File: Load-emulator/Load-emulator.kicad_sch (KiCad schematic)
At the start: 16 parts, among them J1 87832-1420, J2 SSW-126-04-G-D, J3 SSW-126-04-G-D, Q1 TIP41C, U1 LM324A

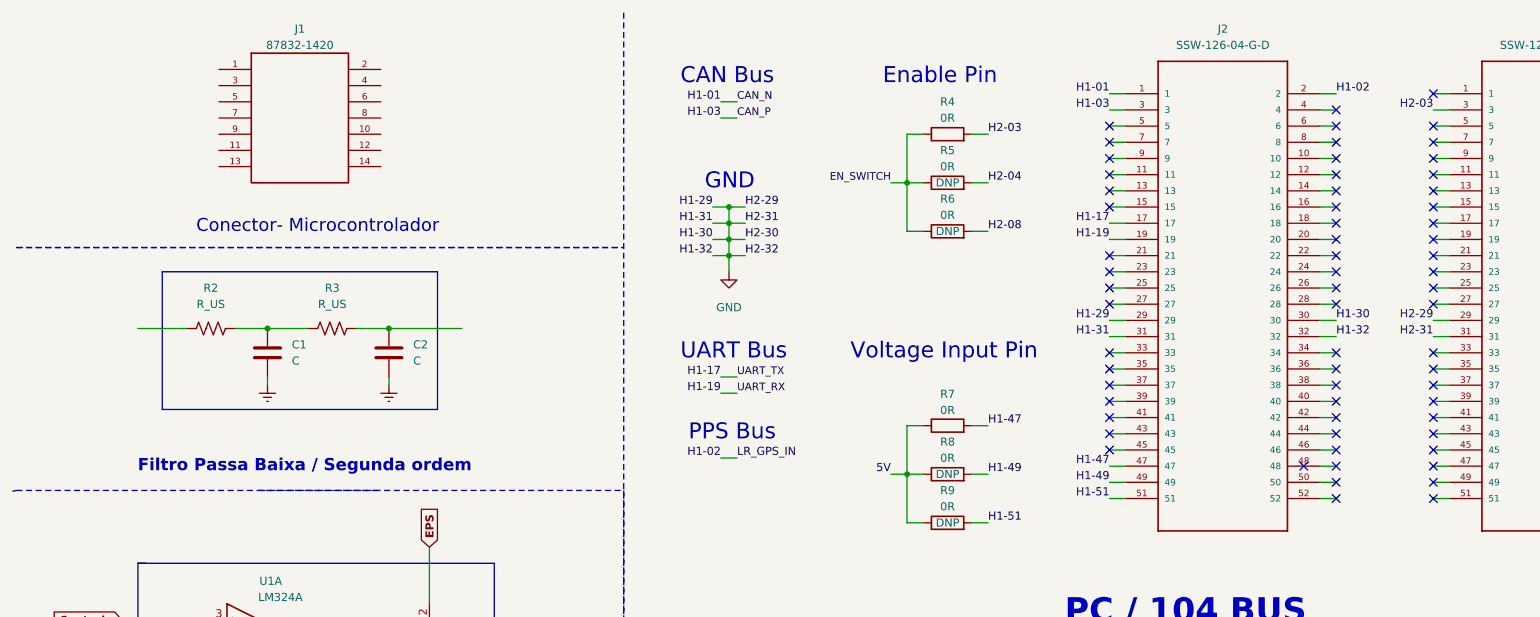
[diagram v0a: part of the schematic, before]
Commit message: Named the connections of PC-104 according to the loads we're trying to emulate
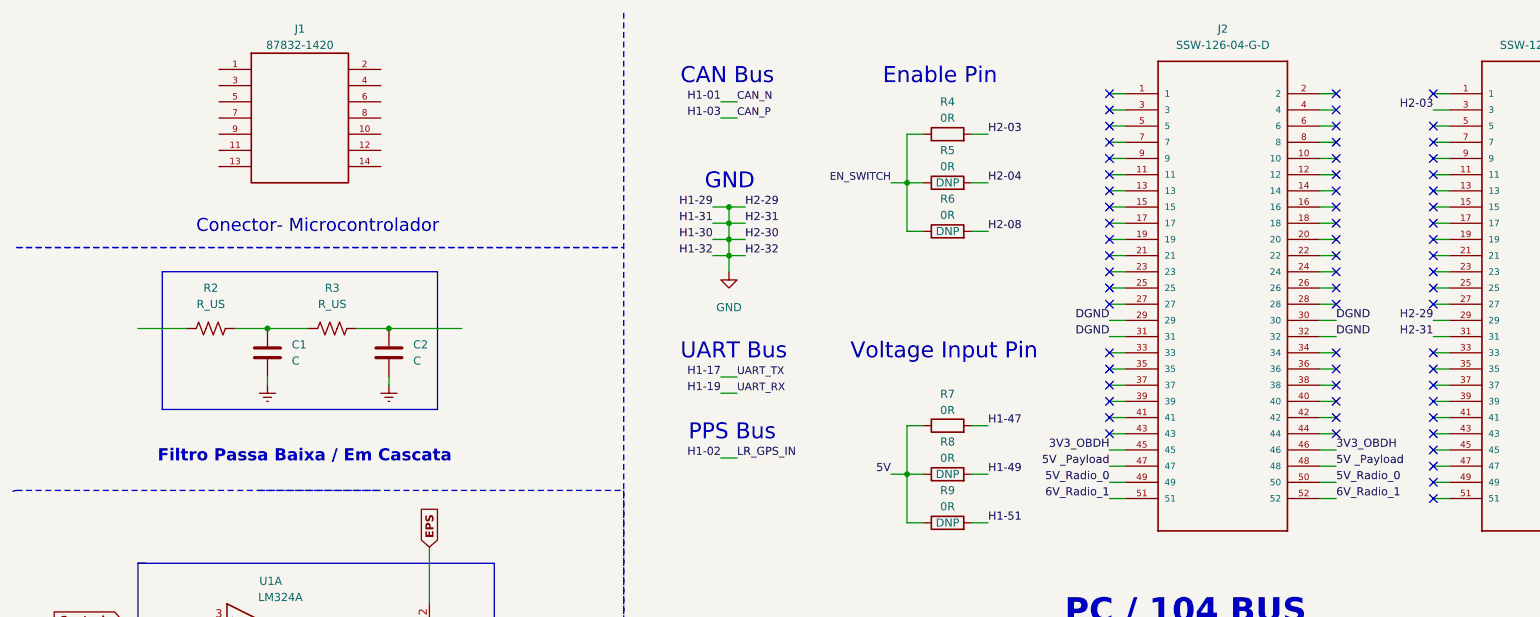
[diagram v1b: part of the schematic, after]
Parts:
- J2: footprint lib:TSW-126-07-X-D -> footprints:SSW-126-01-G-D
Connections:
- net CAN_N: no longer J2.1
- net CAN_P: no longer J2.3
- net GND: no longer J2.29, J2.30, J2.31, J2.32
- net H1-02: no longer J2.2
- net H1-17: no longer J2.17
- net H1-19: no longer J2.19
- net H1-47: no longer J2.47
- net H1-49: no longer J2.49
- net H1-51: no longer J2.51
- net 3V3_OBDH: now reaches J2.45
- net 3V3_OBDH: now also J2.46
- net 5V _Payload: now reaches J2.48
- net 5V _Payload: now also J2.47
- net 5V_Radio_0: now reaches J2.50
- net 5V_Radio_0: now also J2.49
- net 6V_Radio_1: now reaches J2.52
- net 6V_Radio_1: now also J2.51
- new net DGND: J2.29, J2.30, J2.31, J2.32
- no-connect marks 86 -> 85
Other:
- note added: "Filtro Passa Baixa / Em Cascata"
- note removed: "Filtro Passa Baixa / Segunda ordem"
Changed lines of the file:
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@@
 	)
 	(no_connect
-		(at 219.71 83.82)
+		(at 184.15 48.26)
 	)
 	(no_connect
@@
 	)
 	(no_connect
+		(at 184.15 27.94)
+	)
+	(no_connect
 		(at 219.71 73.66)
 	)
@@
 	)
 	(no_connect
-		(at 214.63 83.82)
-	)
-	(no_connect
 		(at 219.71 66.04)
 	)
 	(no_connect
+		(at 184.15 25.4)
+	)
+	(no_connect
 		(at 234.95 83.82)
 	)
@@
 	)
 	(no_connect
+		(at 184.15 45.72)
+	)
+	(no_connect
 		(at 219.71 35.56)
 	)
@@
 	)
 	(no_connect
-		(at 184.15 81.28)
-	)
-	(no_connect
 		(at 219.71 55.88)
 	)
@@
 	)
 	(no_connect
-		(at 219.71 88.9)
-	)
-	(no_connect
 		(at 184.15 68.58)
 	)
@@
 	)
 	(no_connect
+		(at 219.71 25.4)
+	)
+	(no_connect
 		(at 270.51 88.9)
 	)
@@
 	)
 	(no_connect
-		(at 219.71 81.28)
-	)
-	(no_connect
 		(at 234.95 33.02)
 	)
@@
 	(no_connect
 		(at 234.95 35.56)
-	)
-	(no_connect
-		(at 219.71 86.36)
 	)
 	(no_connect
@@
 		)
 	)
-	(text "Filtro Passa Baixa / Segunda ordem\n"
+	(text "Filtro Passa Baixa / Em Cascata\n\n"
 		(exclude_from_sim no)
 		(at 57.912 83.82 0)
@@
 		)
 	)
-	(label "H1-47"
+	(label "5V _Payload"
 		(at 184.15 83.82 180)
 		(fields_autoplaced yes)
@@
 		)
 	)
-	(label "H1-32"
+	(label "DGND"
 		(at 219.71 63.5 0)
 		(fields_autoplaced yes)
@@
 		)
 	)
-	(label "H1-02"
-		(at 219.71 25.4 0)
-		(fields_autoplaced yes)
-		(effects
-			(font
-				(size 1.27 1.27)
-			)
-			(justify left bottom)
-		)
-	)
 	(label "H2-30"
 		(at 270.51 60.96 0)
@@
 		)
 	)
-	(label "H1-49"
+	(label "5V_Radio_0"
 		(at 184.15 86.36 180)
 		(fields_autoplaced yes)
@@
 		)
 	)
-	(label "H1-51"
+	(label "6V_Radio_1"
 		(at 184.15 88.9 180)
 		(fields_autoplaced yes)
@@
 		)
 	)
+	(label "3V3_OBDH"
+		(at 184.15 81.28 180)
+		(fields_autoplaced yes)
+		(effects
+			(font
+				(size 1.27 1.27)
+			)
+			(justify right bottom)
+		)
+	)
 	(label "H1-19"
 		(at 123.19 72.39 180)
@@
 	)
 	(label "H1-17"
-		(at 184.15 45.72 180)
-		(fields_autoplaced yes)
-		(effects
-			(font
-				(size 1.27 1.27)
-			)
-			(justify right bottom)
-		)
-	)
-	(label "H1-17"
 		(at 123.19 69.85 180)
 		(fields_autoplaced yes)
@@
 		)
 	)
+	(label "3V3_OBDH"
+		(at 219.71 81.28 0)
+		(fields_autoplaced yes)
+		(effects
+			(font
+				(size 1.27 1.27)
+			)
+			(justify left bottom)
+		)
+	)
 	(label "H2-04"
 		(at 165.1 39.37 0)
@@
 		)
 	)
-	(label "H1-01"
-		(at 184.15 25.4 180)
-		(fields_autoplaced yes)
-		(effects
-			(font
-				(size 1.27 1.27)
-			)
-			(justify right bottom)
-		)
-	)
-	(label "H1-30"
+	(label "DGND"
 		(at 219.71 60.96 0)
 		(fields_autoplaced yes)
@@
 		)
 	)
-	(label "H1-31"
+	(label "DGND"
 		(at 184.15 63.5 180)
-		(fields_autoplaced yes)
-		(effects
-			(font
-				(size 1.27 1.27)
-			)
-			(justify right bottom)
-		)
-	)
-	(label "H1-03"
-		(at 184.15 27.94 180)
 		(fields_autoplaced yes)
 		(effects
@@
 		)
 	)
-	(label "H1-29"
+	(label "5V_Radio_0"
+		(at 219.71 86.36 0)
+		(fields_autoplaced yes)
+		(effects
+			(font
+				(size 1.27 1.27)
+			)
+			(justify left bottom)
+		)
+	)
+	(label "DGND"
 		(at 184.15 60.96 180)
 		(fields_autoplaced yes)
@@
 		)
 	)
-	(label "H1-19"
-		(at 184.15 48.26 180)
-		(fields_autoplaced yes)
-		(effects
-			(font
-				(size 1.27 1.27)
-			)
-			(justify right bottom)
-		)
-	)
 	(label "CAN_P"
 		(at 125.73 29.21 0)
@@
 		)
 	)
+	(label "5V _Payload"
+		(at 219.71 83.82 0)
+		(fields_autoplaced yes)
+		(effects
+			(font
+				(size 1.27 1.27)
+			)
+			(justify left bottom)
+		)
+	)
 	(label "H2-03"
 		(at 234.95 27.94 180)
@@
 			)
 			(justify right bottom)
+		)
+	)
+	(label "6V_Radio_1"
+		(at 219.71 88.9 0)
+		(fields_autoplaced yes)
+		(effects
+			(font
+				(size 1.27 1.27)
+			)
+			(justify left bottom)
 		)
 	)
@@
 			)
 		)
-		(property "Footprint" "lib:TSW-126-07-X-D"
+		(property "Footprint" "footprints:SSW-126-01-G-D"
 			(at 191.77 25.4 0)
 			(effects

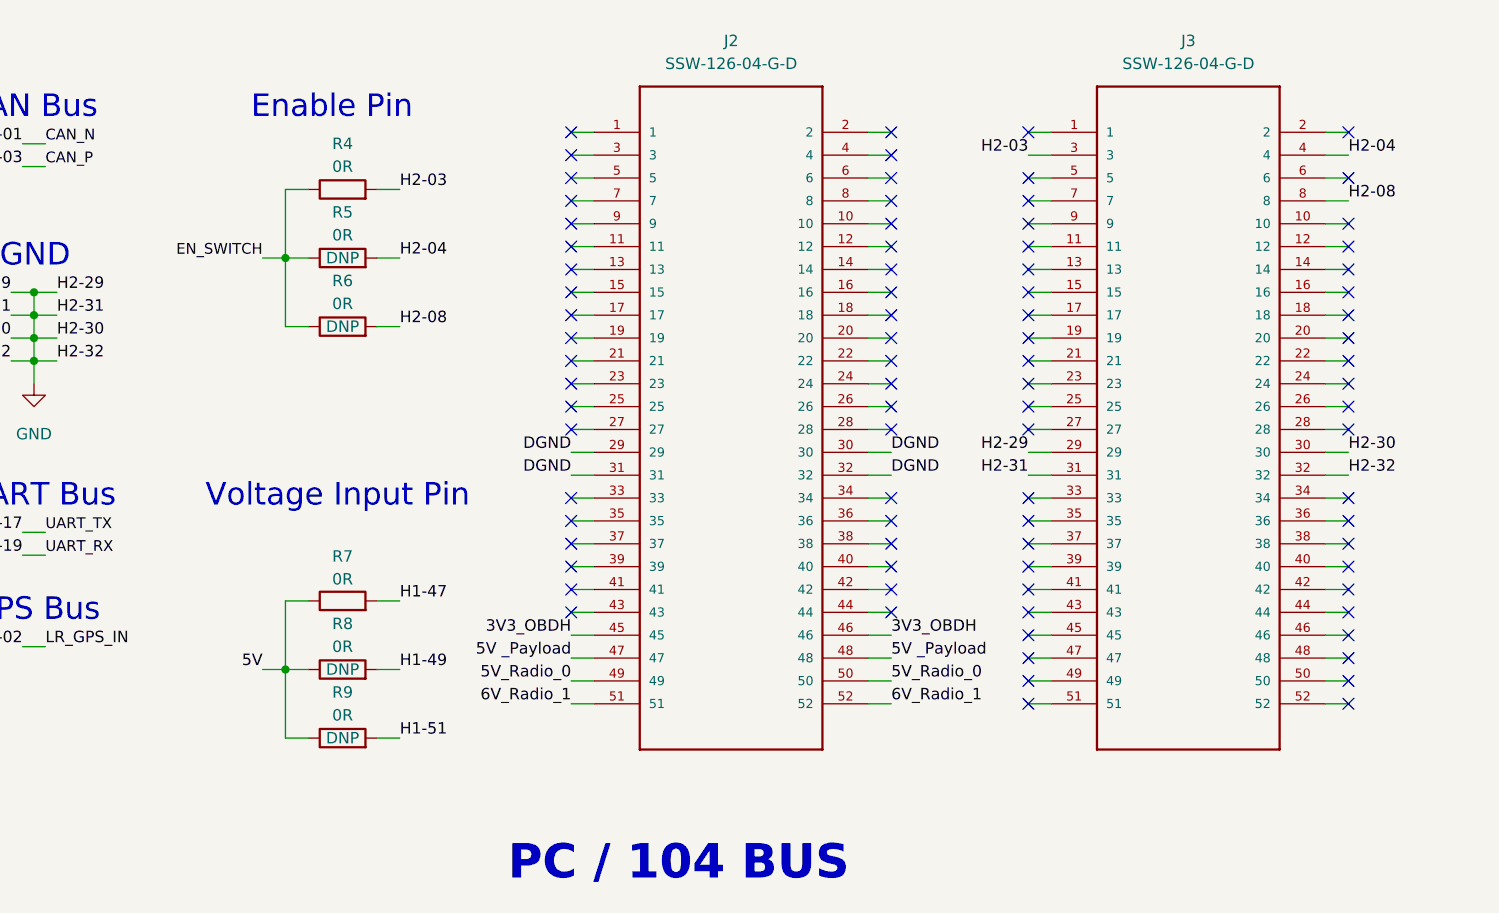
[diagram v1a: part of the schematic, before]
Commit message: Finalização dos rótulos do PC104 e leve reorganização espacial do arquivo
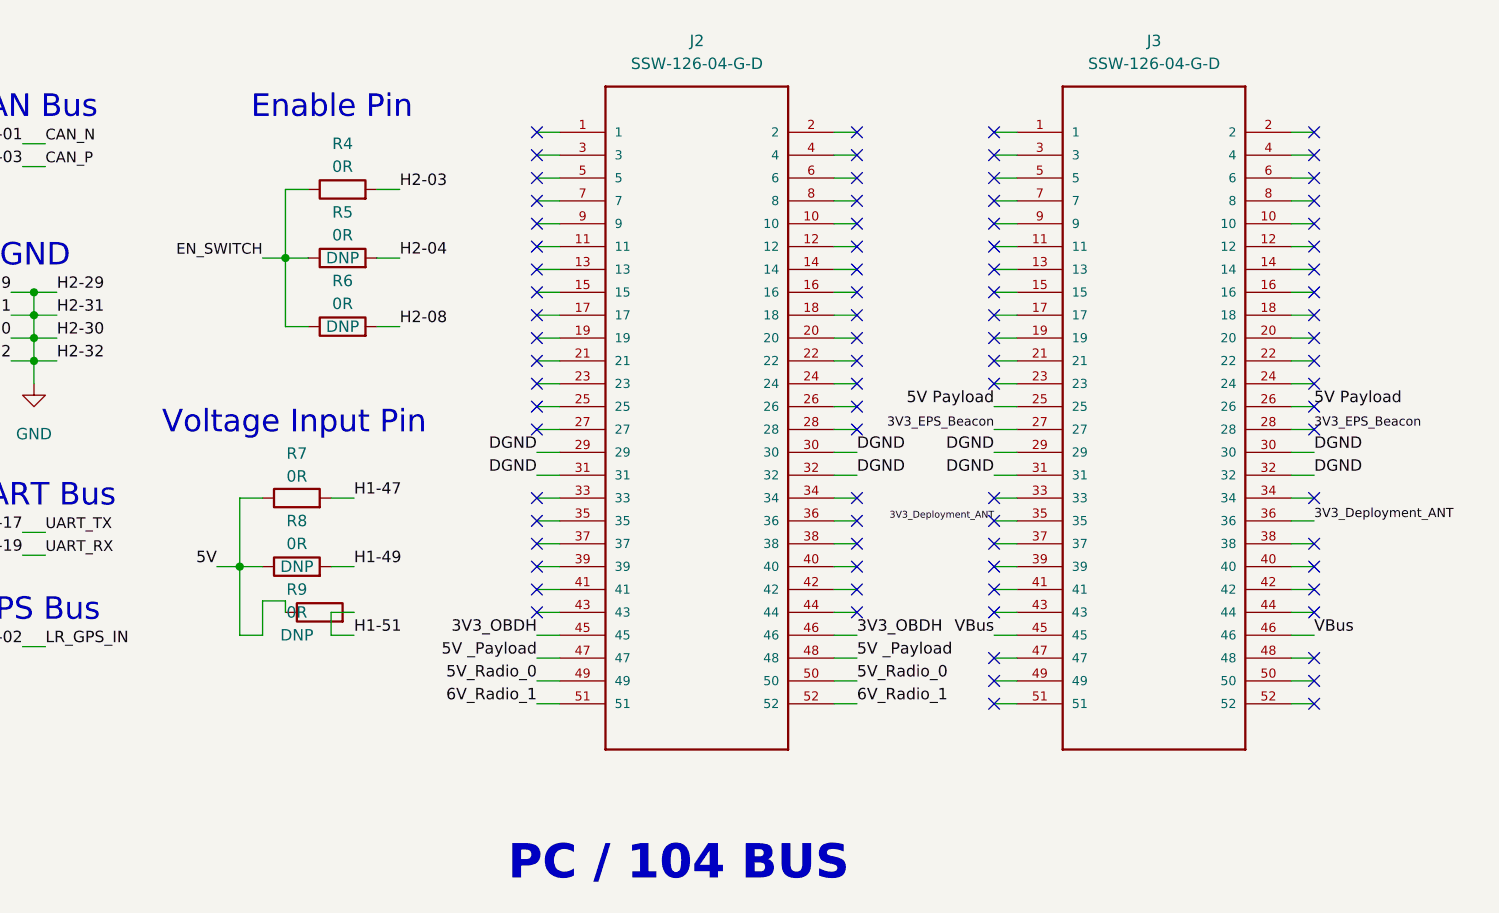
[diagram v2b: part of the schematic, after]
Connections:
- net DGND: now also J3.29, J3.30, J3.31, J3.32
- net GND: no longer J3.29, J3.30, J3.31, J3.32
- net H2-03: no longer J3.3
- net H2-04: no longer J3.4
- net H2-08: no longer J3.8
- net 5V Payload: now reaches J3.25
- net 5V Payload: now also J3.26
- net 3V3_EPS_Beacon: now reaches J3.27
- net 3V3_EPS_Beacon: now also J3.28
- net 3V3_Deployment_ANT: now reaches J3.35
- net 3V3_Deployment_ANT: now also J3.36
- net VBus: now reaches J3.45
- net VBus: now also J3.46
- no-connect marks 85 -> 83
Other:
- moved on the sheet: J2, J3, R7, R8, R9

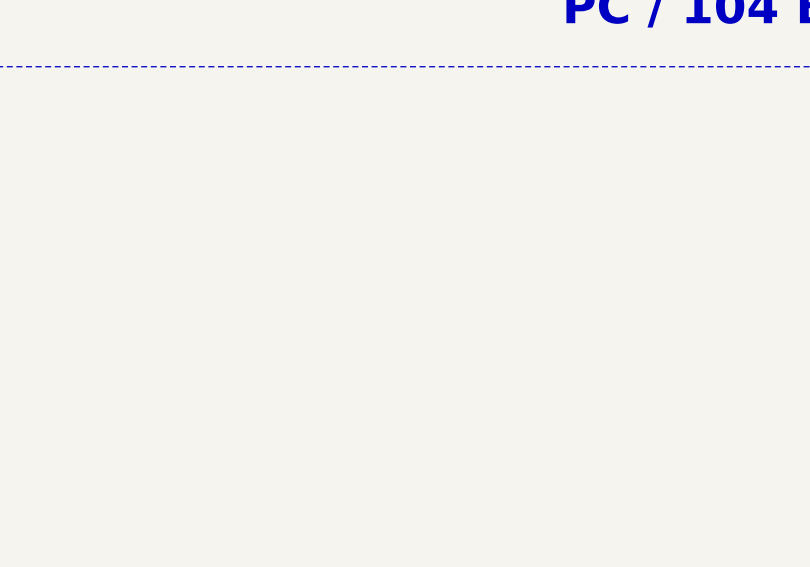
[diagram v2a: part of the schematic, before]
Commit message: Adicionados todos os canais desejados no módulo do current sink, em novas folhas hierárquicas. Falta agora juntar todas as instâncias de folhas duplicadas.
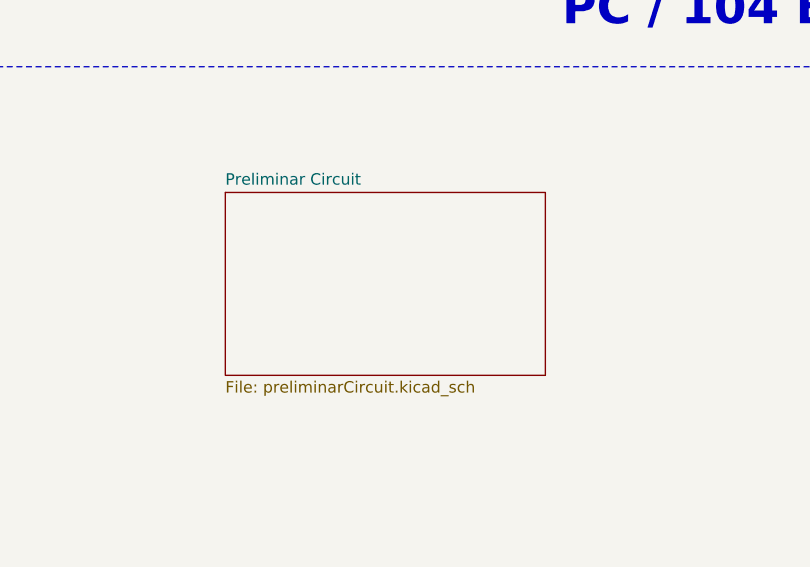
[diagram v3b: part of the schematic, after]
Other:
- added sheet Preliminar Circuit (preliminarCircuit.kicad_sch)
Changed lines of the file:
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@@
+		)
+	)
+	(sheet
+		(at 139.7 127)
+		(size 35.56 20.32)
+		(fields_autoplaced yes)
+		(stroke
+			(width 0.1524)
+			(type solid)
+		)
+		(fill
+			(color 0 0 0 0.0000)
+		)
+		(property "Sheetname" "Preliminar Circuit"
+			(at 139.7 126.2884 0)
+			(effects
+				(font
+					(size 1.27 1.27)
+				)
+				(justify left bottom)
+			)
+		)
+		(property "Sheetfile" "preliminarCircuit.kicad_sch"
+			(at 139.7 147.9046 0)
+			(effects
+				(font
+					(size 1.27 1.27)
+				)
+				(justify left top)
+			)
+		)
+		(instances
+			(project "Load-emulator"
+				(path "/9054bfd2-3cc0-4c96-aa71-abdb09b76dc7"
+					(page "2")
+				)
+			)
 		)
 	)

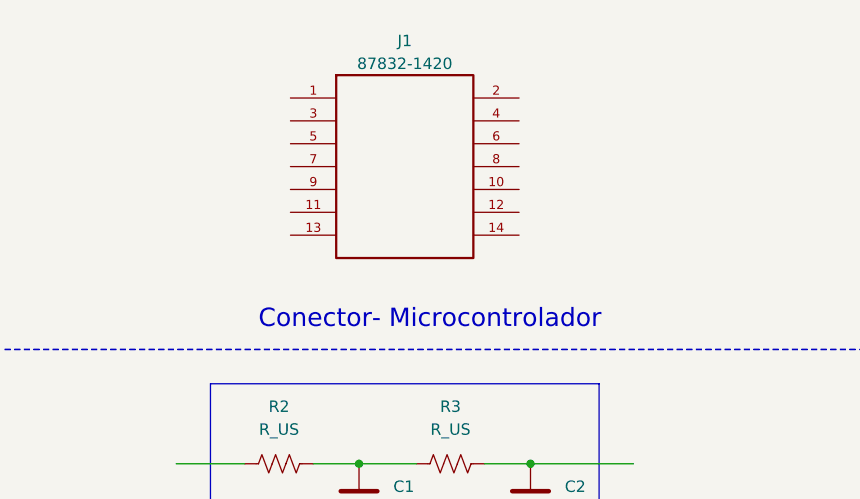
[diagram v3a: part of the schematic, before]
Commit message: Replacement of the microcontroller w/ picoblade
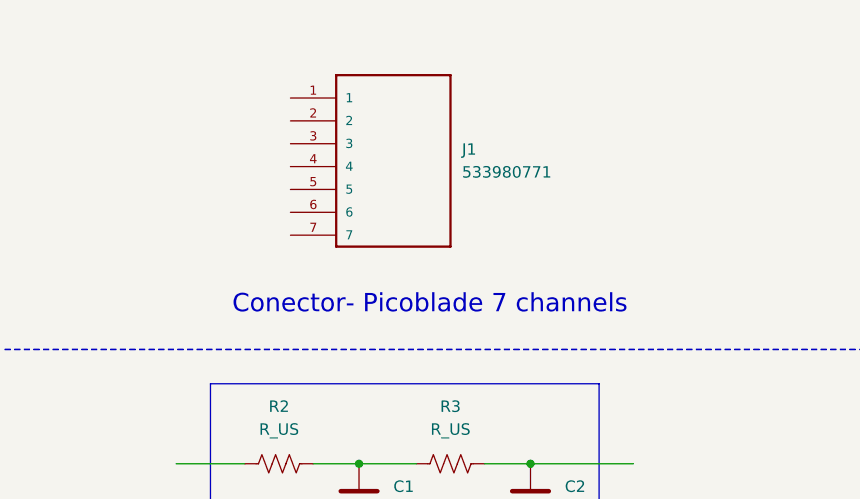
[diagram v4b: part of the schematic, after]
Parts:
- removed J1: 87832-1420, 87832-1420:MOLEX_87832-1420, symbol 87832-1420:87832-1420
- added J1: 533980771, 533980771:MOLEX_533980771, symbol 533980771:533980771
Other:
- note added: "Conector- Picoblade 7 channels"
- note removed: "Conector- Microcontrolador"
